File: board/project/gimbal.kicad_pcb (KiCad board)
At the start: 2 copper layers, 38.1 x 50.8 mm, 8 parts, among them M1 Motor_Servo, M2 Motor_Servo, U1 LM7805_TO220, U2 GY-521, U3 Joystick

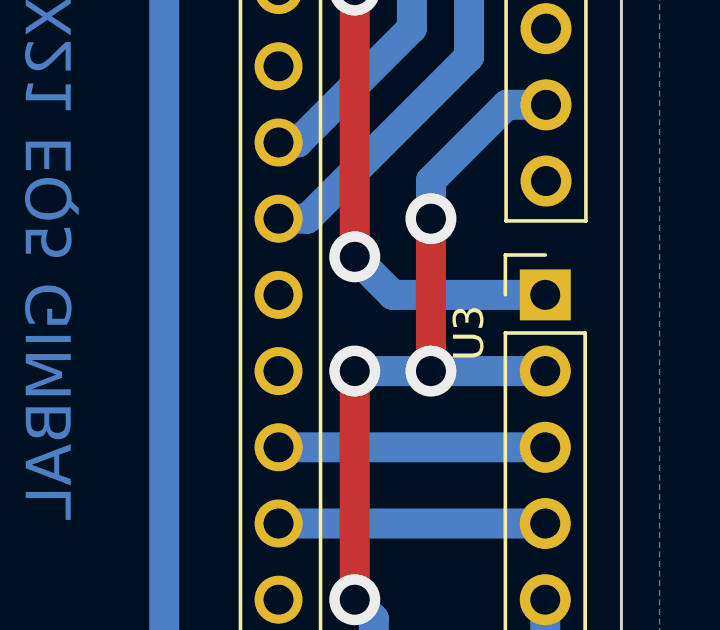
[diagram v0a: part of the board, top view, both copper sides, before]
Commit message: fix joystick power input
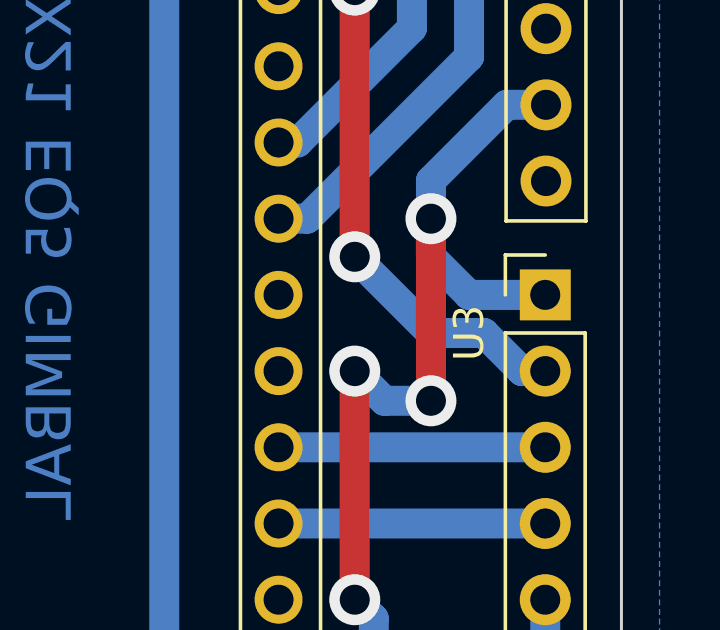
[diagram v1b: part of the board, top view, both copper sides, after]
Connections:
- U3 pad 1: +5V -> Earth
- U3 pad 2: Earth -> +5V
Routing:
- net Earth: track 146.9 -> 150.1 mm
- net +5V: track 36.1 -> 37.2 mm
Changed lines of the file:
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@@
     (fp_line (start -1.27 -0.635) (end -0.635 -1.27) (layer "F.Fab") (width 0.1))
     (pad "1" thru_hole rect (at 0 0) (size 1.7 1.7) (drill 1) (layers *.Cu *.Mask)
-      (net 27 "+5V") (pinfunction "GND") (pintype "power_in"))
+      (net 4 "Earth") (pinfunction "GND") (pintype "power_in"))
     (pad "2" thru_hole oval (at 0 2.54) (size 1.7 1.7) (drill 1) (layers *.Cu *.Mask)
-      (net 4 "Earth") (pinfunction "Vcc") (pintype "power_in"))
+      (net 27 "+5V") (pinfunction "Vcc") (pintype "power_in"))
     (pad "3" thru_hole oval (at 0 5.08) (size 1.7 1.7) (drill 1) (layers *.Cu *.Mask)
       (net 20 "Net-(A1-Pad20)") (pinfunction "X") (pintype "output"))
@@
   )
   (segment (start 160.02 102.87) (end 160.02 95.25) (width 1) (layer "F.Cu") (net 4))
-  (segment (start 162.56 95.25) (end 162.56 90.17) (width 1) (layer "F.Cu") (net 4))
-  (via (at 162.56 95.25) (size 1.7) (drill 1) (layers "F.Cu" "B.Cu") (free) (net 4))
+  (segment (start 162.56 96.2405) (end 162.56 90.17) (width 1) (layer "F.Cu") (net 4))
+  (via (at 162.56 96.2405) (size 1.7) (drill 1) (layers "F.Cu" "B.Cu") (free) (net 4))
   (via (at 162.56 90.17) (size 1.7) (drill 1) (layers "F.Cu" "B.Cu") (free) (net 4))
   (via (at 160.02 102.87) (size 1.7) (drill 1) (layers "F.Cu" "B.Cu") (free) (net 4))
   (via (at 160.02 95.25) (size 1.7) (drill 1) (layers "F.Cu" "B.Cu") (net 4))
   (segment (start 156.21 74.93) (end 157.48 74.93) (width 1) (layer "B.Cu") (net 4))
-  (segment (start 160.02 95.25) (end 162.56 95.25) (width 1) (layer "B.Cu") (net 4))
   (segment (start 138.43 76.2) (end 139.7 77.47) (width 1) (layer "B.Cu") (net 4))
   (segment (start 136.215 76.2) (end 138.43 76.2) (width 1.5) (layer "B.Cu") (net 4))
@@
   (segment (start 162.56 73.66) (end 162.575 73.675) (width 1) (layer "B.Cu") (net 4))
   (segment (start 148.59 74.93) (end 143.51 80.01) (width 1) (layer "B.Cu") (net 4))
+  (segment (start 163.83 92.71) (end 166.37 92.71) (width 1) (layer "B.Cu") (net 4))
+  (segment (start 161.0105 96.2405) (end 160.02 95.25) (width 1) (layer "B.Cu") (net 4))
   (segment (start 140.97 80.01) (end 142.24 80.01) (width 1.5) (layer "B.Cu") (net 4))
   (segment (start 139.7 77.47) (end 139.7 78.74) (width 1.5) (layer "B.Cu") (net 4))
+  (segment (start 162.56 96.2405) (end 161.0105 96.2405) (width 1) (layer "B.Cu") (net 4))
   (segment (start 134.62 76.2) (end 136.215 76.2) (width 1.5) (layer "B.Cu") (net 4))
-  (segment (start 166.37 95.25) (end 162.56 95.25) (width 1) (layer "B.Cu") (net 4))
   (segment (start 156.21 74.93) (end 148.59 74.93) (width 1) (layer "B.Cu") (net 4))
   (segment (start 160.655 109.22) (end 159.385 110.49) (width 1) (layer "B.Cu") (net 4))
@@
   (segment (start 143.51 80.01) (end 142.24 80.01) (width 1) (layer "B.Cu") (net 4))
   (segment (start 155.575 110.49) (end 153.67 108.585) (width 1) (layer "B.Cu") (net 4))
+  (segment (start 162.56 90.17) (end 162.56 91.44) (width 1) (layer "B.Cu") (net 4))
   (segment (start 166.355 86.375) (end 166.395 86.375) (width 1.5) (layer "B.Cu") (net 4))
   (segment (start 162.575 73.675) (end 166.395 73.675) (width 1) (layer "B.Cu") (net 4))
+  (segment (start 162.56 91.44) (end 163.83 92.71) (width 1) (layer "B.Cu") (net 4))
   (segment (start 152.4 113.03) (end 146.05 106.68) (width 1) (layer "B.Cu") (net 5))
   (segment (start 163.83 113.03) (end 152.4 113.03) (width 1) (layer "B.Cu") (net 5))
@@
   (via (at 160.02 77.47) (size 1.7) (drill 1) (layers "F.Cu" "B.Cu") (free) (net 27))
   (segment (start 160.02 80.01) (end 160.02 77.47) (width 1) (layer "B.Cu") (net 27))
+  (segment (start 165.595245 95.25) (end 164.325245 93.98) (width 1) (layer "B.Cu") (net 27))
+  (segment (start 166.37 95.25) (end 165.595245 95.25) (width 1) (layer "B.Cu") (net 27))
   (segment (start 160.02 82.55) (end 160.02 80.01) (width 1) (layer "B.Cu") (net 27))
   (segment (start 157.48 80.01) (end 160.02 80.01) (width 1) (layer "B.Cu") (net 27))
-  (segment (start 160.02 91.44) (end 161.29 92.71) (width 1) (layer "B.Cu") (net 27))
-  (segment (start 161.29 92.71) (end 166.37 92.71) (width 1) (layer "B.Cu") (net 27))
+  (segment (start 162.56 93.98) (end 160.02 91.44) (width 1) (layer "B.Cu") (net 27))
+  (segment (start 164.325245 93.98) (end 162.56 93.98) (width 1) (layer "B.Cu") (net 27))
   (segment (start 166.38 71.12) (end 166.395 71.135) (width 1) (layer "B.Cu") (net 27))
   (segment (start 160.02 71.12) (end 166.38 71.12) (width 1) (layer "B.Cu") (net 27))
